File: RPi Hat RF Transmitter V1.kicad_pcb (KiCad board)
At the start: 4 copper layers, 65 x 56 mm, 67 parts, among them CON1 Sig_In, CON2 SMA-, CON3 Sig_In, CON4 Sig_In, CON5 SMA-, IC1 HMC241AQS16E, IC2 HMC241AQS16E, IC3 SN74HC139PW, J1 Conn_01x04_Male, J2 Conn_01x04_Male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

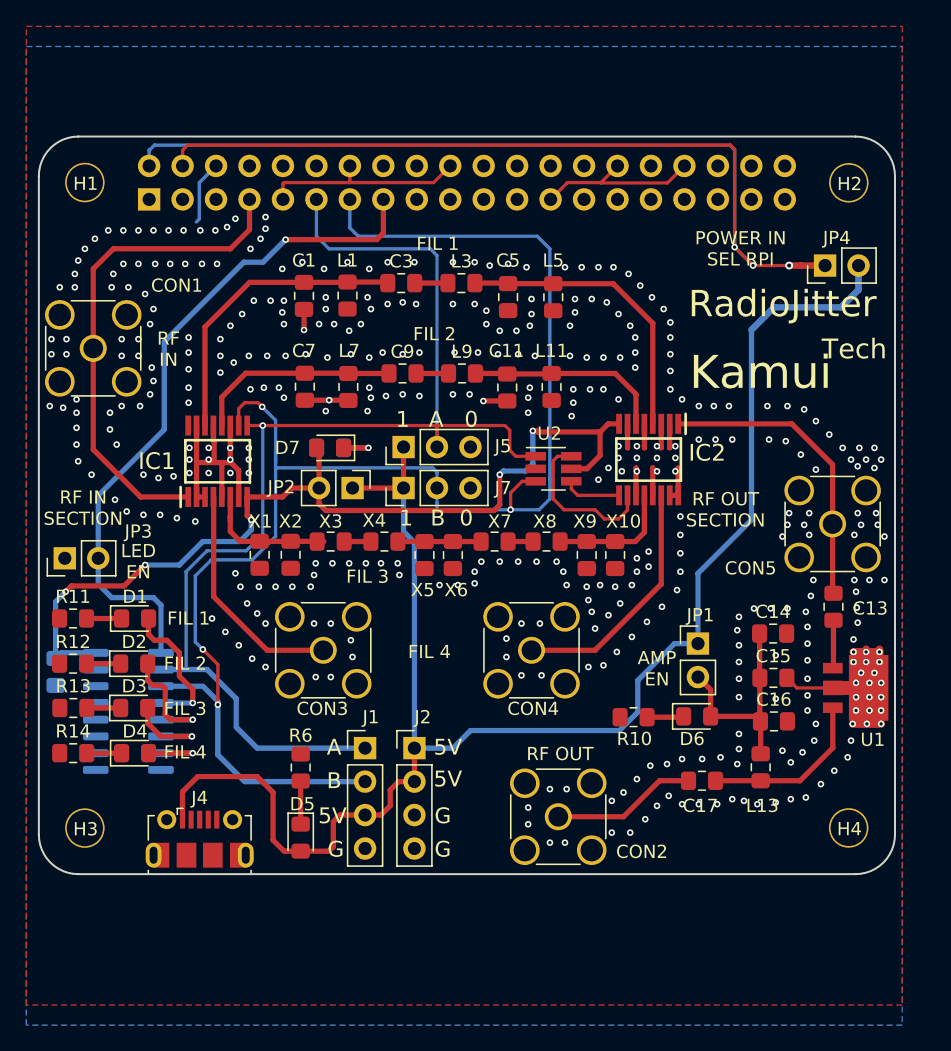
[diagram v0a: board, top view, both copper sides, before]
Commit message: removes digital switch and puts mechanical switch
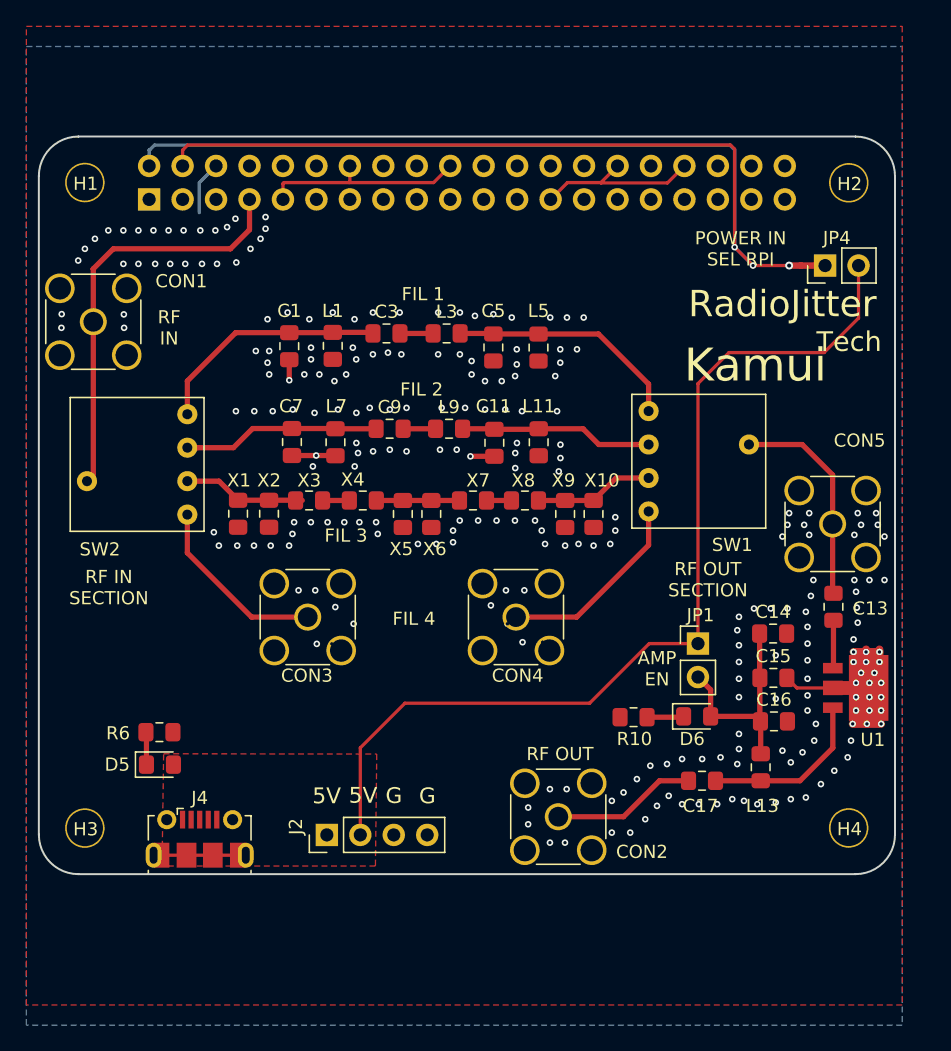
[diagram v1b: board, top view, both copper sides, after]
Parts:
- removed C19: 0.1uF, Capacitor_SMD:C_0805_2012Metric_Pad1.15x1.40mm_HandSolder
- removed D1, D2, D3, D4, D7: LED, LED_SMD:LED_0805_2012Metric_Pad1.15x1.40mm_HandSolder
- removed IC1, IC2: HMC241AQS16E, SamacSys_Parts:SOP64P600X175-16N
- removed IC3: SN74HC139PW, Package_SO:SOIC-16_3.9x9.9mm_P1.27mm
- removed J1: Conn_01x04_Male, Connector_PinHeader_2.54mm:PinHeader_1x04_P2.54mm_Vertical
- removed J5, J7: Conn_01x03_Male, Connector_PinHeader_2.54mm:PinHeader_1x03_P2.54mm_Vertical
- removed JP2, JP3: Jumper, Connector_PinHeader_2.54mm:PinHeader_1x02_P2.54mm_Vertical
- removed R11, R12, R13, R14, R15: 330, Resistor_SMD:R_0805_2012Metric_Pad1.15x1.40mm_HandSolder
- removed U2: 74AUC2G04, Package_TO_SOT_SMD:SOT-23-6_Handsoldering
- added SW1: SW_Coded, VK_Cus_KiCad:1x4_switch, F.Cu at (127.4, 84.2)
- added SW2: SW_Coded, VK_Cus_KiCad:1x4_switch, F.Cu at (87.3, 87.0)
- C1, C5: value C -> 62pF
- C3: value C -> 3.3pF
- D5, D6: value LED -> Red
- L1, L5: value L -> 18nH
- L3: value L -> 330nH
- moved D5 12.0 mm to (87.7, 108.5), turned to 0 degrees
- moved R6 11.1 mm to (87.7, 106.0), turned to 180 degrees
- moved J2 9.36 mm to (100.4, 113.8), turned to 90 degrees
- moved C11 4.31 mm to (113.1, 84.1)
- moved C9 4.31 mm to (105.2, 83.0)
- moved L9 4.31 mm to (109.7, 83.0)
- moved C7 4.31 mm to (97.8, 84.0)
- moved L7 4.31 mm to (101.1, 84.0)
- moved L11 4.31 mm to (116.5, 84.0)
- moved C1 3.98 mm to (97.6, 76.7)
- moved C3 3.98 mm to (104.9, 75.8)
- moved L3 3.98 mm to (109.5, 75.8)
- moved L1 3.98 mm to (100.9, 76.7)
- moved C5 3.98 mm to (113.1, 76.8)
- moved L5 3.98 mm to (116.5, 76.8)
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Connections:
- net GPIO4 renamed RF_IN_SWITCH
- J3 pad 11: GPIO17 -> Net-(J3-Pad11)
- J3 pad 13: GPIO27 -> Net-(J3-Pad13)
- J3 pad 15: GPIO22 -> Net-(J3-Pad15)
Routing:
- net GPIO27: track 118.1 -> 0.00 mm, vias 4 -> 0
- net GPIO17: track 94.4 -> 0.00 mm, vias 1 -> 0
- net RF_SWITCH_PWR: track 70.4 -> 0.00 mm, vias 5 -> 0
- net GPIO22: track 52.1 -> 0.00 mm, vias 1 -> 0
- net +5V: track 121.2 -> 73.5 mm
- net GND: track 91.6 -> 63.2 mm, vias 399 -> 247
- net Net-(IC2-Pad10): track 12.1 -> 0.00 mm
- net SEL_RF1: track 10.8 -> 0.00 mm, vias 1 -> 0
- net SEL_RF2: track 9.50 -> 0.00 mm, vias 1 -> 0
- net SEL_RF3: track 7.28 -> 0.00 mm, vias 1 -> 0
- net RF_ANT_OUT: track 22.8 -> 16.3 mm
- net RF_IN_SWITCH: track 37.8 -> 31.7 mm
- net SEL_RF4: track 5.77 -> 0.00 mm, vias 1 -> 0
- net RF1_OUT: track 22.8 -> 18.2 mm
- net RF1_IN: track 22.4 -> 17.9 mm
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- added copper zone on F.Cu, net +5V
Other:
- net class Default: clearance 0.2 -> 0.4
- rule trace_clearance: 0.2 -> 0.4
- board text removed: "0"
- board text removed: "1"
- board text removed: "2"
- board text removed: "3"
- board text removed: "4"
- board text removed: "74AUC2G04"
- board text removed: "A"
- board text removed: "B"
- board text removed: "FIL"
- board text removed: "HMC241"
- board text removed: "IC1, IC2"
- board text removed: "IC3"
- board text removed: "JP1"
- board text removed: "JP2"
- board text removed: "JP3"
- board text removed: "JP4"
- board text removed: "LED EN"
- board text removed: "RF SWITCH EN"
- board text removed: "SBB5089Z"
- board text removed: "SN74HC139"
- board text removed: "U1"
- board text removed: "U2"

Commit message: goes on proto production here
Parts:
- added FL4: LFCN-180, Filter:Filter_Mini-Circuits_FV1206, F.Cu at (107.1, 97.5)
- added JP2: Jumper, Connector_PinHeader_2.54mm:PinHeader_1x02_P2.54mm_Vertical, F.Cu at (85.7, 68.8)
- added JP3: Jumper, Connector_PinHeader_2.54mm:PinHeader_1x02_P2.54mm_Vertical, F.Cu at (136.2, 83.9)
- moved CON4 2.64 mm to (117.4, 97.5)
- moved CON3 1.97 mm to (97.0, 97.5)
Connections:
- J3 pad 7: RF_IN_SWITCH -> RF_RPI
- SW1 pad 1: RF_ANT_OUT -> Net-(JP3-Pad1)
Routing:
- net RF_IN_SWITCH: track 31.7 -> 17.7 mm
- net RF_RPI: track 0.00 -> 8.68 mm
- net RF4_OUT: track 14.1 -> 21.6 mm
- net RF4_IN: track 14.9 -> 22.4 mm, vias 1 -> 0
- net Net-(JP3-Pad1): track 0.00 -> 4.94 mm
- net RF_ANT_OUT: track 16.3 -> 11.8 mm
- net +5V: track 73.5 -> 74.2 mm
- net GND: vias 247 -> 208
- net /P5V_HAT: vias 3 -> 2
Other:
- copper layers 4 -> 2
- net class Default: clearance 0.4 -> 0.2
- rule trace_clearance: 0.4 -> 0.2
- board text removed: "If you want to use an SMT 40-pin header, please move the top edge up by 0.5mm and locate the header in the same location as the current TH part."
- board text removed: "This is a HAT compatible PCB starting design based on the official Raspberry Pi specs at: https://github.com/raspberrypi/hats/blob/master/designguide.md Currently the camera slot and display cutout are not here. See the schematic for the details on the EEPROM and power setup. This board does have the correct components for powering the Pi via the HAT. If you need the Pi to provide 5V or 3.3V, ple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"
